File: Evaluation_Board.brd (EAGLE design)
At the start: 60.9 x 39.4 mm, 38 parts, among them IC1 MEGA32-A, IC2 FT232RL, IC3 317EMP, J1 DCJ0202, Q1 16 MHz

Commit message: Port A beschriftet
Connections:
- net N$10 renamed A3
- net N$11 renamed A2
- net N$12 renamed A1
- net N$13 renamed A0
- net N$6 renamed A7
- net N$7 renamed A6
- net N$8 renamed A5
- net N$9 renamed A4
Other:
- board text added: "+5V"
- board text added: "A0"
- board text added: "A1"
- board text added: "A2"
- board text added: "A3"
- board text added: "A4"
- board text added: "A5"
- board text added: "A6"
- board text added: "A7"
- board text added: "Reset"
- board text added: "Rx"
- board text added: "Tx"
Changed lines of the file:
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@@
 März 2015 v1.0</text>
 <circle x="55.88" y="16.51" radius="0.354975" width="0" layer="25"/>
+<text x="14.12875" y="33.81375" size="1.016" layer="25">Rx</text>
+<text x="16.66875" y="33.81375" size="1.016" layer="25">Tx</text>
+<text x="30.95625" y="34.13125" size="1.016" layer="25">Reset</text>
+<text x="28.41625" y="34.13125" size="1.016" layer="25">+5V</text>
+<text x="34.925" y="33.9725" size="1.016" layer="25">A0</text>
+<text x="37.465" y="33.9725" size="1.016" layer="25">A1</text>
+<text x="40.005" y="33.9725" size="1.016" layer="25">A2</text>
+<text x="42.545" y="33.9725" size="1.016" layer="25">A3</text>
+<text x="45.085" y="33.9725" size="1.016" layer="25">A4</text>
+<text x="47.625" y="33.9725" size="1.016" layer="25">A5</text>
+<text x="50.165" y="33.9725" size="1.016" layer="25">A6</text>
+<text x="52.705" y="33.9725" size="1.016" layer="25">A7</text>
 </plain>
 <attributes>
@@
 <wire x1="58.4175" y1="6.45" x2="58.2" y2="6.6675" width="0.3048" layer="1"/>
 </signal>
-<signal name="N$6">
+<signal name="A7">
 <contactref element="IC1" pad="30"/>
 <contactref element="SV2" pad="1"/>
@@
 <wire x1="53.6575" y1="36.5125" x2="47.625" y2="30.48" width="0.3048" layer="1"/>
 </signal>
-<signal name="N$7">
+<signal name="A6">
 <contactref element="IC1" pad="31"/>
 <contactref element="SV2" pad="2"/>
@@
 <wire x1="51.1175" y1="36.5125" x2="46.99" y2="32.385" width="0.3048" layer="1"/>
 </signal>
-<signal name="N$8">
+<signal name="A5">
 <contactref element="SV2" pad="3"/>
 <contactref element="IC1" pad="32"/>
@@
 <wire x1="46.355" y1="34.29" x2="48.5775" y2="36.5125" width="0.3048" layer="1"/>
 </signal>
-<signal name="N$9">
+<signal name="A4">
 <contactref element="IC1" pad="33"/>
 <contactref element="SV2" pad="4"/>
@@
 <wire x1="44.535" y1="25.59" x2="45.275" y2="25.59" width="0.3048" layer="1"/>
 </signal>
-<signal name="N$10">
+<signal name="A3">
 <contactref element="IC1" pad="34"/>
 <contactref element="SV2" pad="5"/>
@@
 <wire x1="42.735" y1="31.6225" x2="43.4975" y2="32.385" width="0.3048" layer="1"/>
 </signal>
-<signal name="N$11">
+<signal name="A2">
 <contactref element="IC1" pad="35"/>
 <contactref element="SV2" pad="6"/>
@@
 <wire x1="41.91" y1="27.415" x2="41.935" y2="27.39" width="0.3048" layer="1"/>
 </signal>
-<signal name="N$12">
+<signal name="A1">
 <contactref element="IC1" pad="36"/>
 <contactref element="SV2" pad="7"/>
@@
 <wire x1="41.135" y1="27.39" x2="41.135" y2="31.255" width="0.3048" layer="1"/>
 </signal>
-<signal name="N$13">
+<signal name="A0">
 <contactref element="IC1" pad="37"/>
 <contactref element="SV2" pad="8"/>
@@
 <via x="44.1325" y="31.115" extent="1-16" drill="0.5"/>
 <via x="42.2275" y="33.3375" extent="1-16" drill="0.5"/>
-<via x="39.6875" y="34.29" extent="1-16" drill="0.5"/>
+<via x="39.52875" y="34.29" extent="1-16" drill="0.5"/>
 <via x="48.5775" y="32.7025" extent="1-16" drill="0.5"/>
-<via x="47.3075" y="33.9725" extent="1-16" drill="0.5"/>
+<via x="47.14875" y="33.81375" extent="1-16" drill="0.5"/>
 <via x="47.3075" y="21.9075" extent="1-16" drill="0.5"/>
 <via x="52.3875" y="6.0325" extent="1-16" drill="0.5"/>
@@
 <via x="26.9875" y="10.16" extent="1-16" drill="0.5"/>
 <via x="33.655" y="29.21" extent="1-16" drill="0.5"/>
-<via x="44.45" y="33.9725" extent="1-16" drill="0.5"/>
-<via x="50.165" y="34.29" extent="1-16" drill="0.5"/>
+<via x="44.60875" y="33.655" extent="1-16" drill="0.5"/>
+<via x="49.53" y="33.655" extent="1-16" drill="0.5"/>
 <via x="59.53125" y="18.57375" extent="1-16" drill="0.5"/>
 <via x="59.69" y="2.54" extent="1-16" drill="0.5"/>

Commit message: Alle Beschriftungen eingefuegt
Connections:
- net N$31 renamed C2
- net N$32 renamed C3
- net N$33 renamed C4
- net N$34 renamed C5
- net N$35 renamed C6
- net N$36 renamed C7
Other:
- board text added: "B1"
- board text added: "C2"
- board text added: "C3"
- board text added: "C4"
- board text added: "C5"
- board text added: "C6"
- board text added: "C7"
- board text added: "CTS"
- board text added: "D6"
- board text added: "GND"
- board text added: "INT0"
- board text added: "INT1"
- board text added: "INT2"
- board text added: "MISO"
- board text added: "MOSI"
- board text added: "OC0"
- board text added: "OC1A"
- board text added: "OC1B"
- board text added: "OC2"
- board text added: "RTS"
- board text added: "SCK"
- board text added: "SCL"
- board text added: "SDA"
- board text added: "SS"
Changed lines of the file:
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@@
 März 2015 v1.0</text>
 <circle x="55.88" y="16.51" radius="0.354975" width="0" layer="25"/>
-<text x="14.12875" y="33.81375" size="1.016" layer="25">Rx</text>
-<text x="16.66875" y="33.81375" size="1.016" layer="25">Tx</text>
-<text x="30.95625" y="34.13125" size="1.016" layer="25">Reset</text>
-<text x="28.41625" y="34.13125" size="1.016" layer="25">+5V</text>
-<text x="34.925" y="33.9725" size="1.016" layer="25">A0</text>
-<text x="37.465" y="33.9725" size="1.016" layer="25">A1</text>
-<text x="40.005" y="33.9725" size="1.016" layer="25">A2</text>
-<text x="42.545" y="33.9725" size="1.016" layer="25">A3</text>
-<text x="45.085" y="33.9725" size="1.016" layer="25">A4</text>
-<text x="47.625" y="33.9725" size="1.016" layer="25">A5</text>
-<text x="50.165" y="33.9725" size="1.016" layer="25">A6</text>
-<text x="52.705" y="33.9725" size="1.016" layer="25">A7</text>
+<text x="14.12875" y="33.81375" size="1.016" layer="25" font="vector">Rx</text>
+<text x="16.66875" y="33.81375" size="1.016" layer="25" font="vector">Tx</text>
+<text x="31.4325" y="34.13125" size="0.6096" layer="25" font="vector">Reset</text>
+<text x="29.05125" y="34.13125" size="0.6096" layer="25" font="vector">+5V</text>
+<text x="34.925" y="33.9725" size="1.016" layer="25" font="vector">A0</text>
+<text x="37.465" y="33.9725" size="1.016" layer="25" font="vector">A1</text>
+<text x="40.005" y="33.9725" size="1.016" layer="25" font="vector">A2</text>
+<text x="42.545" y="33.9725" size="1.016" layer="25" font="vector">A3</text>
+<text x="45.085" y="33.9725" size="1.016" layer="25" font="vector">A4</text>
+<text x="47.625" y="33.9725" size="1.016" layer="25" font="vector">A5</text>
+<text x="50.165" y="33.9725" size="1.016" layer="25" font="vector">A6</text>
+<text x="52.705" y="33.9725" size="1.016" layer="25" font="vector">A7</text>
+<text x="13.97" y="4.28625" size="1.016" layer="25" font="vector">B1</text>
+<text x="16.66875" y="4.28625" size="0.6096" layer="25" font="vector">INT2</text>
+<text x="19.20875" y="4.28625" size="0.6096" layer="25" font="vector">INT1</text>
+<text x="21.59" y="4.28625" size="0.6096" layer="25" font="vector">INT0</text>
+<text x="24.13" y="4.28625" size="0.6096" layer="25" font="vector">OC2</text>
+<text x="26.3525" y="4.28625" size="0.6096" layer="25" font="vector">OC1B</text>
+<text x="28.73375" y="4.28625" size="0.6096" layer="25" font="vector">OC1A</text>
+<text x="31.90875" y="4.28625" size="0.6096" layer="25" font="vector">OC0</text>
+<text x="35.40125" y="4.28625" size="0.6096" layer="25" font="vector">SCL</text>
+<text x="37.7825" y="4.28625" size="0.6096" layer="25" font="vector">SDA</text>
+<text x="40.3225" y="4.28625" size="1.016" layer="25" font="vector">C2</text>
+<text x="42.8625" y="4.28625" size="1.016" layer="25" font="vector">C3</text>
+<text x="45.4025" y="4.28625" size="1.016" layer="25" font="vector">C4</text>
+<text x="47.9425" y="4.28625" size="1.016" layer="25" font="vector">C5</text>
+<text x="50.4825" y="4.28625" size="1.016" layer="25" font="vector">C6</text>
+<text x="53.0225" y="4.28625" size="1.016" layer="25" font="vector">C7</text>
+<text x="19.20875" y="34.13125" size="0.6096" layer="25" font="vector">CTS</text>
+<text x="21.74875" y="34.13125" size="0.6096" layer="25" font="vector">RTS</text>
+<text x="24.13" y="33.655" size="1.016" layer="25" font="vector">D6</text>
+<text x="26.67" y="34.13125" size="0.6096" layer="25" font="vector">GND</text>
+<text x="49.37125" y="9.04875" size="0.8128" layer="25" font="vector">SCK</text>
+<text x="48.895" y="11.58875" size="0.8128" layer="25" font="vector">MISO</text>
+<text x="48.895" y="14.12875" size="0.8128" layer="25" font="vector">MOSI</text>
+<text x="50.165" y="16.8275" size="0.8128" layer="25" font="vector">SS</text>
 </plain>
 <attributes>
@@
 </element>
 <element name="C3" library="rcl" package="C0805" value="100n" x="29.05125" y="31.90875" smashed="yes">
-<attribute name="NAME" x="27.78125" y="33.17875" size="0.8128" layer="25"/>
+<attribute name="NAME" x="25.87625" y="31.90875" size="0.8128" layer="25"/>
 <attribute name="VALUE" x="27.78125" y="29.36875" size="1.27" layer="27"/>
 </element>
@@
 <via x="39.52875" y="34.29" extent="1-16" drill="0.5"/>
 <via x="48.5775" y="32.7025" extent="1-16" drill="0.5"/>
-<via x="47.14875" y="33.81375" extent="1-16" drill="0.5"/>
+<via x="47.3075" y="33.9725" extent="1-16" drill="0.5"/>
 <via x="47.3075" y="21.9075" extent="1-16" drill="0.5"/>
 <via x="52.3875" y="6.0325" extent="1-16" drill="0.5"/>
 <via x="24.765" y="5.3975" extent="1-16" drill="0.5"/>
-<via x="20.955" y="5.08" extent="1-16" drill="0.5"/>
+<via x="21.43125" y="5.715" extent="1-16" drill="0.5"/>
 <via x="53.975" y="21.9075" extent="1-16" drill="0.5"/>
 <via x="49.2125" y="29.845" extent="1-16" drill="0.5"/>
@@
 <via x="8.255" y="4.1275" extent="1-16" drill="0.5"/>
 <via x="1.905" y="3.81" extent="1-16" drill="0.5"/>
-<via x="17.78" y="4.7625" extent="1-16" drill="0.5"/>
 <via x="19.05" y="6.0325" extent="1-16" drill="0.5"/>
 <via x="26.9875" y="7.9375" extent="1-16" drill="0.5"/>
@@
 <via x="58.42" y="1.27" extent="1-16" drill="0.5"/>
 <via x="8.89" y="1.27" extent="1-16" drill="0.5"/>
-<via x="14.9225" y="5.08" extent="1-16" drill="0.5"/>
+<via x="14.2875" y="7.77875" extent="1-16" drill="0.5"/>
 <via x="1.27" y="15.24" extent="1-16" drill="0.5"/>
 <via x="2.54" y="15.24" extent="1-16" drill="0.5"/>
@@
 <via x="23.495" y="22.86" extent="1-16" drill="0.5"/>
 <via x="20.32" y="15.875" extent="1-16" drill="0.5"/>
-<via x="23.1775" y="33.655" extent="1-16" drill="0.5"/>
+<via x="23.33625" y="33.17875" extent="1-16" drill="0.5"/>
 <via x="24.92375" y="33.17875" extent="1-16" drill="0.5"/>
 </signal>
@@
 <wire x1="49.0825" y1="24.6325" x2="50.1675" y2="25.7175" width="0.3048" layer="1"/>
 </signal>
-<signal name="N$31">
+<signal name="C2">
 <contactref element="IC1" pad="21"/>
 <contactref element="SV5" pad="6"/>
@@
 <wire x1="41.935" y1="15.79" x2="41.935" y2="4.47" width="0.3048" layer="1"/>
 </signal>
-<signal name="N$32">
+<signal name="C3">
 <contactref element="IC1" pad="22"/>
 <contactref element="SV5" pad="5"/>
@@
 <wire x1="43.815" y1="3.81" x2="43.815" y2="2.54" width="0.3048" layer="1"/>
 </signal>
-<signal name="N$33">
+<signal name="C4">
 <contactref element="IC1" pad="23"/>
 <contactref element="SV5" pad="4"/>
@@
 <wire x1="46.355" y1="17.145" x2="46.355" y2="2.54" width="0.3048" layer="1"/>
 </signal>
-<signal name="N$34">
+<signal name="C5">
 <contactref element="IC1" pad="24"/>
 <contactref element="SV5" pad="3"/>
@@
 <wire x1="47.9425" y1="3.4925" x2="48.895" y2="2.54" width="0.3048" layer="1"/>
 </signal>
-<signal name="N$35">
+<signal name="C6">
 <contactref element="IC1" pad="25"/>
 <contactref element="SV5" pad="2"/>
@@
 <wire x1="51.435" y1="3.81" x2="51.435" y2="2.54" width="0.3048" layer="1"/>
 </signal>
-<signal name="N$36">
+<signal name="C7">
 <contactref element="IC1" pad="26"/>
 <contactref element="SV5" pad="1"/>

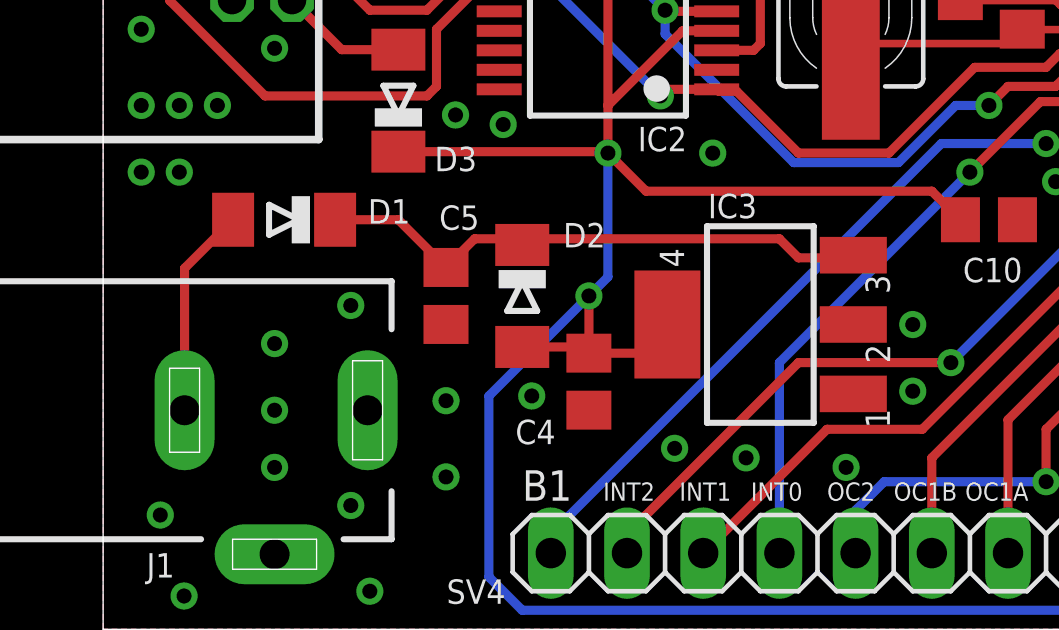
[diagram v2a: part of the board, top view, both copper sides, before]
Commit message: DC Jack geaendert
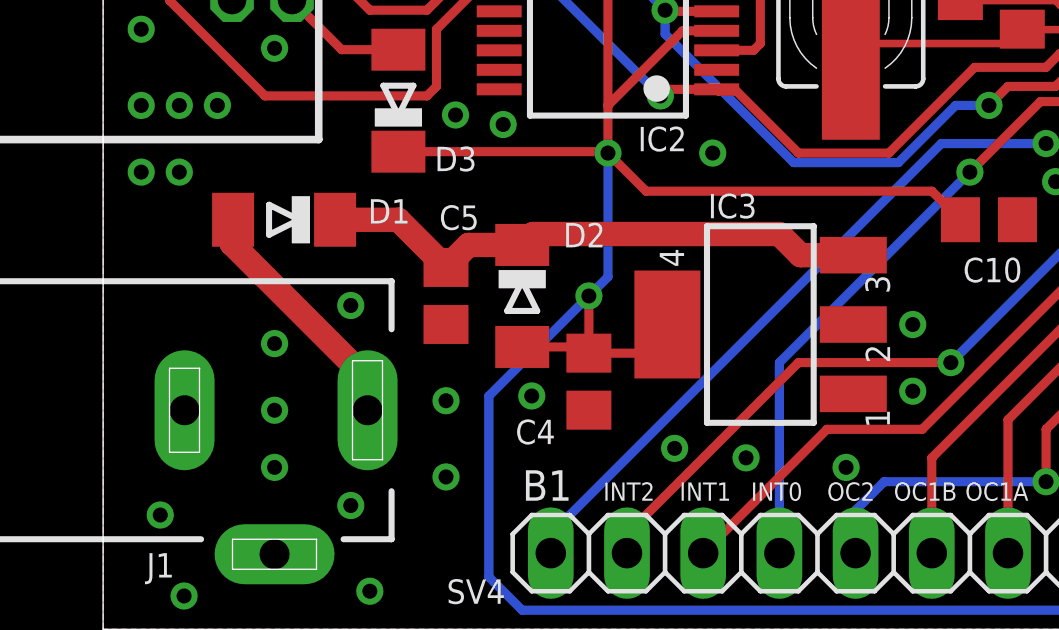
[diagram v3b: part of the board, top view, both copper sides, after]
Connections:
- removed net N$3: D1.A, J1.3
- new net N$2: D1.A, J1.1
- net GND: now also J1.3; no longer J1.1
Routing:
- net N$2: track 0.00 -> 8.25 mm
- net N$3: track 7.02 -> 0.00 mm
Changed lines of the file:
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@@
 <layer number="45" name="Holes" color="7" fill="1" visible="no" active="yes"/>
 <layer number="46" name="Milling" color="3" fill="1" visible="no" active="yes"/>
-<layer number="47" name="Measures" color="7" fill="1" visible="yes" active="yes"/>
+<layer number="47" name="Measures" color="7" fill="1" visible="no" active="yes"/>
 <layer number="48" name="Document" color="7" fill="1" visible="no" active="yes"/>
 <layer number="49" name="Reference" color="7" fill="1" visible="no" active="yes"/>
@@
 <contactref element="C5" pad="2"/>
 <contactref element="IC3" pad="3"/>
-<wire x1="7.7325" y1="13.6525" x2="9.84" y2="13.6525" width="0.3048" layer="1"/>
-<wire x1="9.84" y1="13.6525" x2="11.43" y2="12.0625" width="0.3048" layer="1"/>
-<wire x1="11.43" y1="12.0625" x2="12.385" y2="13.0175" width="0.3048" layer="1"/>
-<wire x1="22.5425" y1="13.0175" x2="23.1775" y2="12.3825" width="0.3048" layer="1"/>
-<wire x1="23.1775" y1="12.3825" x2="25.7175" y2="12.3825" width="0.3048" layer="1"/>
 <wire x1="25.7175" y1="12.3825" x2="25.6286" y2="12.4714" width="0.3048" layer="1"/>
 <wire x1="25.6286" y1="12.4714" x2="25.0063" y2="12.4714" width="0.3048" layer="1"/>
 <contactref element="D2" pad="C"/>
-<wire x1="12.385" y1="13.0175" x2="13.765" y2="13.0175" width="0.3048" layer="1"/>
 <wire x1="13.765" y1="13.0175" x2="13.97" y2="12.8125" width="0.3048" layer="1"/>
-<wire x1="22.5425" y1="13.0175" x2="14.175" y2="13.0175" width="0.3048" layer="1"/>
 <wire x1="14.175" y1="13.0175" x2="13.97" y2="12.8125" width="0.3048" layer="1"/>
+<wire x1="7.7325" y1="13.6525" x2="9.84" y2="13.6525" width="0.8128" layer="1"/>
+<wire x1="9.84" y1="13.6525" x2="11.43" y2="12.0625" width="0.8128" layer="1"/>
+<wire x1="11.43" y1="12.0625" x2="12.18" y2="12.8125" width="0.8128" layer="1"/>
+<wire x1="12.18" y1="12.8125" x2="13.97" y2="12.8125" width="0.8128" layer="1"/>
+<wire x1="14.175" y1="13.0175" x2="14.33375" y2="13.17625" width="0.8128" layer="1"/>
+<wire x1="14.33375" y1="13.17625" x2="22.5425" y2="13.17625" width="0.8128" layer="1"/>
+<wire x1="22.5425" y1="13.17625" x2="23.24735" y2="12.4714" width="0.8128" layer="1"/>
+<wire x1="23.24735" y1="12.4714" x2="25.0063" y2="12.4714" width="0.8128" layer="1"/>
 </signal>
 <signal name="N$5">
@@
 <contactref element="LED1" pad="C"/>
 <contactref element="C5" pad="1"/>
-<contactref element="J1" pad="1"/>
-<contactref element="J1" pad="2"/>
 <contactref element="S3" pad="3"/>
 <contactref element="S3" pad="4"/>
@@
 <via x="23.33625" y="33.17875" extent="1-16" drill="0.5"/>
 <via x="24.92375" y="33.17875" extent="1-16" drill="0.5"/>
+<contactref element="J1" pad="2"/>
+<contactref element="J1" pad="3"/>
 </signal>
 <signal name="+5V">
@@
 <wire x1="34.925" y1="29.5275" x2="35.56" y2="29.5275" width="0.3048" layer="16"/>
 </signal>
-<signal name="N$3">
-<contactref element="J1" pad="3"/>
-<contactref element="D1" pad="A"/>
-<wire x1="2.715" y1="7.3025" x2="2.715" y2="12.035" width="0.3048" layer="1"/>
-<wire x1="2.715" y1="12.035" x2="4.3325" y2="13.6525" width="0.3048" layer="1"/>
-</signal>
 <signal name="N$1">
 <contactref element="D3" pad="A"/>
@@
 <wire x1="25.4635" y1="19.52625" x2="24.92375" y2="18.9865" width="0.254" layer="1"/>
 </signal>
+<signal name="N$2">
+<contactref element="J1" pad="1"/>
+<contactref element="D1" pad="A"/>
+<wire x1="8.815" y1="7.3025" x2="8.815" y2="8.33" width="0.8128" layer="1"/>
+<wire x1="8.815" y1="8.33" x2="4.28625" y2="12.85875" width="0.8128" layer="1"/>
+<wire x1="4.28625" y1="12.85875" x2="4.28625" y2="13.60625" width="0.8128" layer="1"/>
+<wire x1="4.28625" y1="13.60625" x2="4.3325" y2="13.6525" width="0.8128" layer="1"/>
+</signal>
 </signals>
